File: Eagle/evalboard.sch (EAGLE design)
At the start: 5 parts, among them X1 MAC64L

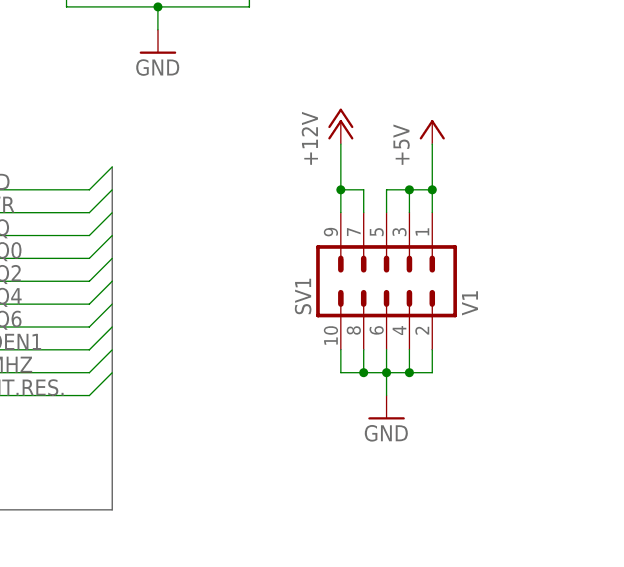
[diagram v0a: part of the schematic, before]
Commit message: Schematic and layout changes
Added two additional tantal caps for 5V and 12V lines.
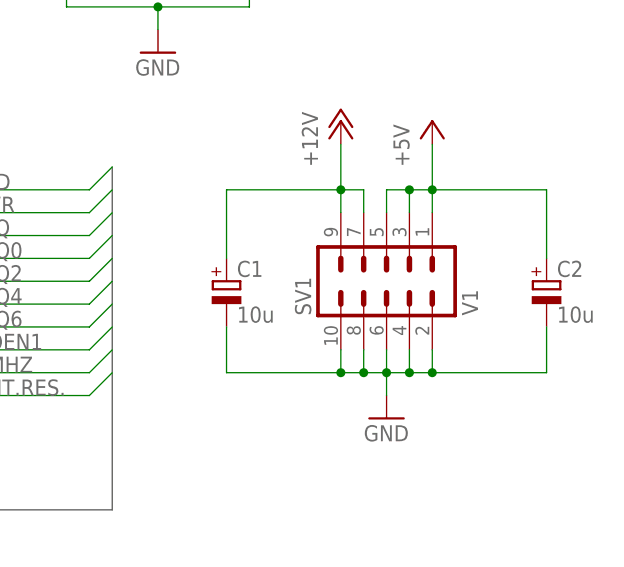
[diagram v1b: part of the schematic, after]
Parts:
- added C1, C2: 10u, rcl:CPOL-EUE2.5-5
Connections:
- net +12V: now also C1.+
- net +5V: now also C2.+
- net GND: now also C1.-, C2.-
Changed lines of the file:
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@@
 <part name="P+2" library="supply1" deviceset="+5V" device=""/>
 <part name="GND4" library="supply1" deviceset="GND" device=""/>
+<part name="C1" library="rcl" deviceset="CPOL-EU" device="E2.5-5" value="10u"/>
+<part name="C2" library="rcl" deviceset="CPOL-EU" device="E2.5-5" value="10u"/>
 </parts>
 <sheets>
@@
 <instance part="P+2" gate="1" x="157.48" y="50.8"/>
 <instance part="GND4" gate="1" x="127" y="58.42"/>
+<instance part="C1" gate="G$1" x="134.62" y="33.02"/>
+<instance part="C2" gate="G$1" x="170.18" y="33.02"/>
 </instances>
 <busses>
@@
 <pinref part="GND1" gate="1" pin="GND"/>
 <wire x1="152.4" y1="20.32" x2="152.4" y2="22.86" width="0.1524" layer="91"/>
+<pinref part="C1" gate="G$1" pin="-"/>
+<wire x1="134.62" y1="27.94" x2="134.62" y2="22.86" width="0.1524" layer="91"/>
+<wire x1="134.62" y1="22.86" x2="147.32" y2="22.86" width="0.1524" layer="91"/>
+<junction x="147.32" y="22.86"/>
+<pinref part="C2" gate="G$1" pin="-"/>
+<wire x1="170.18" y1="27.94" x2="170.18" y2="22.86" width="0.1524" layer="91"/>
+<wire x1="170.18" y1="22.86" x2="157.48" y2="22.86" width="0.1524" layer="91"/>
+<junction x="157.48" y="22.86"/>
 </segment>
 <segment>
@@
 <wire x1="157.48" y1="48.26" x2="157.48" y2="43.18" width="0.1524" layer="91"/>
 <junction x="157.48" y="43.18"/>
+<pinref part="C2" gate="G$1" pin="+"/>
+<wire x1="170.18" y1="35.56" x2="170.18" y2="43.18" width="0.1524" layer="91"/>
+<wire x1="170.18" y1="43.18" x2="157.48" y2="43.18" width="0.1524" layer="91"/>
 </segment>
 </net>
@@
 <wire x1="147.32" y1="48.26" x2="147.32" y2="43.18" width="0.1524" layer="91"/>
 <junction x="147.32" y="43.18"/>
+<pinref part="C1" gate="G$1" pin="+"/>
+<wire x1="134.62" y1="35.56" x2="134.62" y2="43.18" width="0.1524" layer="91"/>
+<wire x1="134.62" y1="43.18" x2="147.32" y2="43.18" width="0.1524" layer="91"/>
 </segment>
 </net>
